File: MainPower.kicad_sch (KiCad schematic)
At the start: 25 parts, among them Q29 MBT2222ADW1T1, Q30 MBT2222ADW1T1, U17 TPS54226PWPR, U18 ADM1176-1ARMZ-R7

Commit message: temp
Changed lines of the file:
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@@
 		)
 	)
-	(hierarchical_label "SDA_BUS"
+	(hierarchical_label "SCL"
 		(shape bidirectional)
-		(at 256.54 130.81 0)
+		(at 256.54 128.27 0)
 		(fields_autoplaced yes)
 		(effects
@@
 		)
 	)
-	(hierarchical_label "SCL_BUS"
+	(hierarchical_label "SDA"
 		(shape bidirectional)
-		(at 256.54 128.27 0)
+		(at 256.54 130.81 0)
 		(fields_autoplaced yes)
 		(effects

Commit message: v1 done
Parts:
- C58, C59: value 100u -> 10u
- U17: symbol Mainboard:TPS54226PWPR -> Argus-IC:TPS54226PWPR
- U18: symbol Mainboard:ADM1176-1ARMZ-R7 -> Argus-IC:ADM1176-1ARMZ-R7
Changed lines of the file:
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@@
 	)
 	(symbol
-		(lib_id "Mainboard:ADM1176-1ARMZ-R7")
+		(lib_id "Argus-IC:ADM1176-1ARMZ-R7")
 		(at 189.23 128.27 0)
 		(unit 1)
@@
 			)
 		)
-		(property "Value" "100u"
+		(property "Value" "10u"
 			(at 37.592 114.808 0)
 			(effects
@@
 			)
 		)
-		(property "Value" "100u"
+		(property "Value" "10u"
 			(at 47.752 114.808 0)
 			(effects
@@
 	)
 	(symbol
-		(lib_id "Mainboard:TPS54226PWPR")
+		(lib_id "Argus-IC:TPS54226PWPR")
 		(at 87.63 127 0)
 		(unit 1)

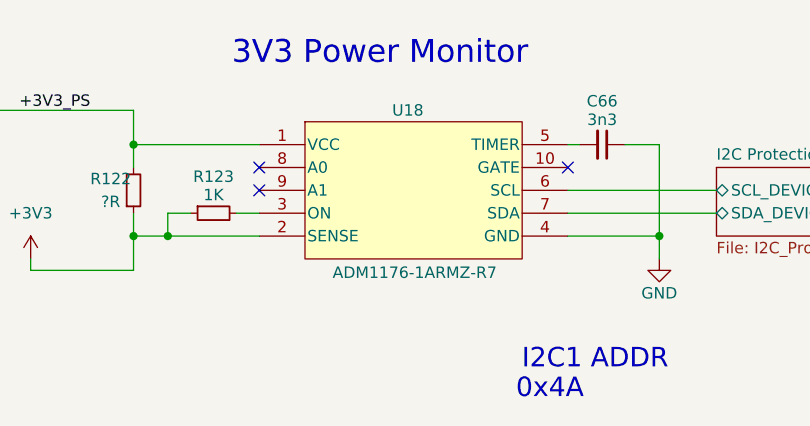
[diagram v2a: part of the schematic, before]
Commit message: Updated i2c device addresses and mcu caps
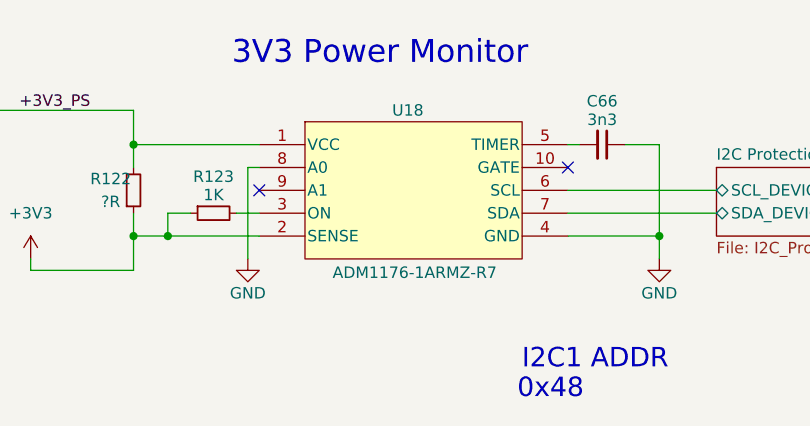
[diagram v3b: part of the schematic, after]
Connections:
- net GND: now also U18.8 (A0)
- no-connect marks 3 -> 2
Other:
- note added: "0x48"
- note removed: "0x4A"
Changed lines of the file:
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@@
 		(at 207.01 125.73)
 	)
-	(no_connect
-		(at 172.72 125.73)
-	)
 	(wire
 		(pts
@@
 	(wire
 		(pts
+			(xy 171.45 125.73) (xy 171.45 135.89)
+		)
+		(stroke
+			(width 0)
+			(type default)
+		)
+	)
+	(wire
+		(pts
 			(xy 142.24 45.72) (xy 142.24 46.99)
 		)
@@
 		(pts
 			(xy 217.17 123.19) (xy 217.17 133.35)
+		)
+		(stroke
+			(width 0)
+			(type default)
+		)
+	)
+	(wire
+		(pts
+			(xy 172.72 125.73) (xy 171.45 125.73)
 		)
 		(stroke
@@
 		)
 	)
-	(text "0x4A"
+	(text "0x48"
 		(exclude_from_sim no)
 		(at 208.788 151.638 0)
@@
 					(unit 1)
 				)
+			)
+		)
+	)
+	(symbol
+		(lib_id "power:GND")
+		(at 171.45 135.89 0)
+		(unit 1)
+		(exclude_from_sim no)
+		(in_bom yes)
+		(on_board yes)
+		(dnp no)
+		(property "Reference" "#PWR0155"
+			(at 171.45 142.24 0)
+			(effects
+				(font
+					(size 1.27 1.27)
+				)
+				(hide yes)
+			)
+		)
+		(property "Value" "GND"
+			(at 171.45 139.7 0)
+			(effects
+				(font
+					(size 1.27 1.27)
+				)
+			)
+		)
+		(property "Footprint" ""
+			(at 171.45 135.89 0)
+			(effects
+				(font
+					(size 1.27 1.27)
+				)
+				(hide yes)
+			)
+		)
+		(property "Datasheet" ""
+			(at 171.45 135.89 0)
+			(effects
+				(font
+					(size 1.27 1.27)
+				)
+				(hide yes)
+			)
+		)
+		(property "Description" "Power symbol creates a global label with name \"GND\" , ground"
+			(at 171.45 135.89 0)
+			(effects
+				(font
+					(size 1.27 1.27)
+				)
+				(hide yes)
+			)
+		)
+		(pin "1"
+		)
+		(instances
+			(project "Avionics-MainBoard"
+				(path "/4c932743-8c6f-426e-9c1f-5a3f2b32c70d/60aa2943-2df4-4541-853f-c25e8e58a8ce"
+					(reference "#PWR0155")
+					(unit 1)
+				)

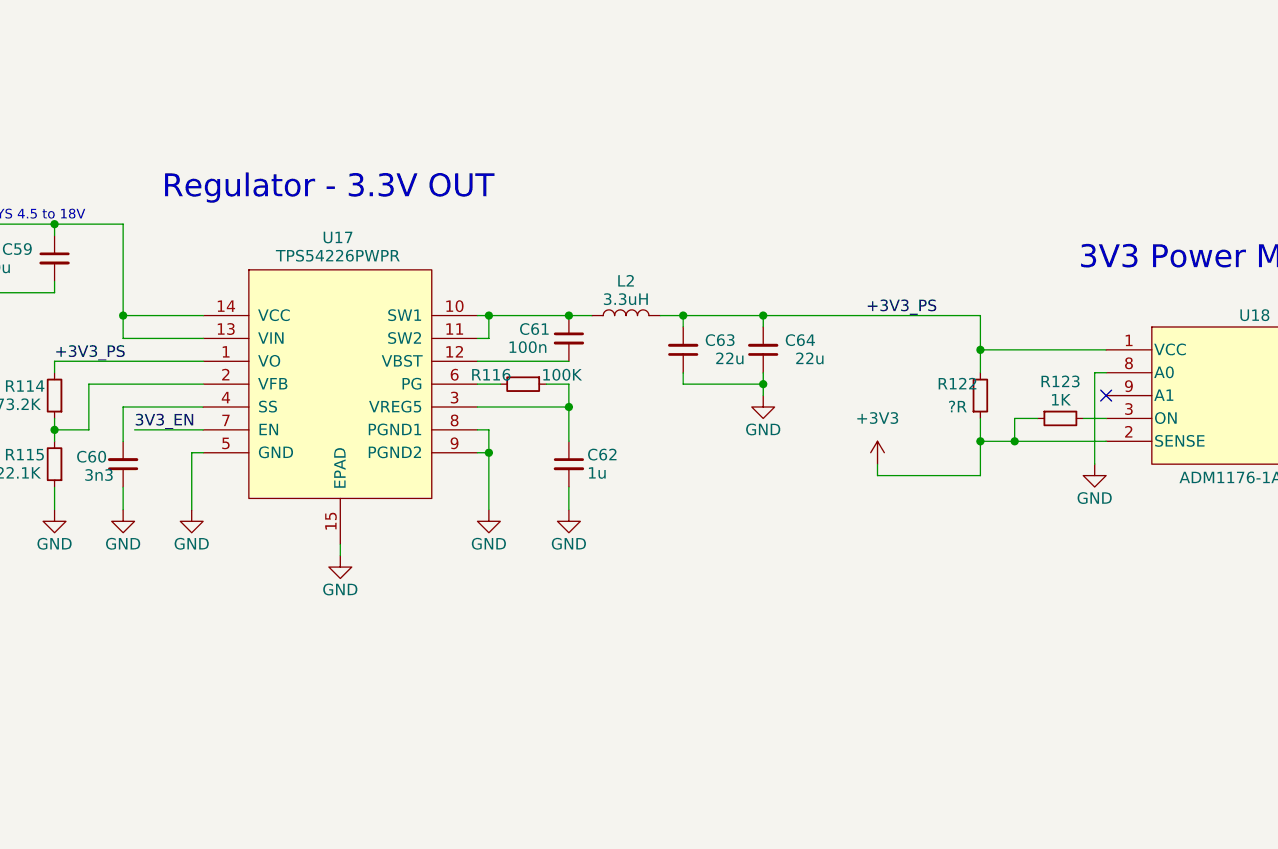
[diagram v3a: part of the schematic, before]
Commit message: Added better protection to SD card, Jetson IO, and added address breakouts to power monitors
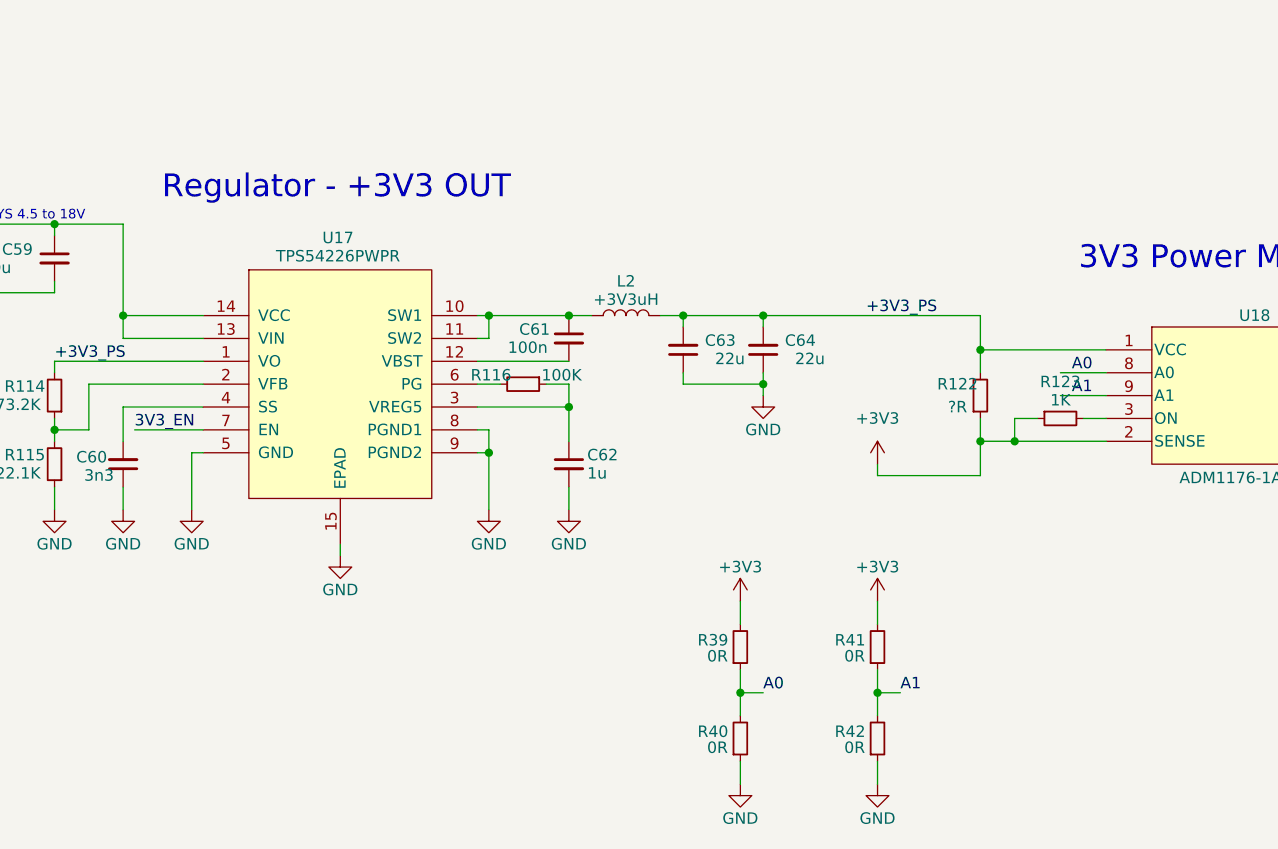
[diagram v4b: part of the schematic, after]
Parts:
- added R39, R40, R41, R42: 0R, Resistor_SMD:R_0603_1608Metric, symbol Device:R_Small
- L2: value 3.3uH -> +3V3uH
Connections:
- net +3V3: now also R39.2, R41.2
- net GND: now also R40.1, R42.1; no longer U18.8 (A0)
- net A1: now reaches U18.9 (A1)
- net A1: now also R41.1, R42.2
- new net A0: R39.1, R40.2, U18.8 (A0)
- no-connect marks 2 -> 1
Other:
- note added: "Regulator - +3V3 OUT"
- note removed: "Regulator - 3.3V OUT"

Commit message: Updated version to v2.1
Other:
- company: (none) -> Carnegie Mellon University
- title: (none) -> Argus Mainboard
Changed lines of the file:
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@@
 	(generator_version "8.0")
 	(paper "A4")
+	(title_block
+		(title "Argus Mainboard")
+		(date "2024-11-19")
+		(rev "v2.1")
+		(company "Carnegie Mellon University")
+		(comment 1 "M. Holliday")
+		(comment 2 "N. Khera")
+		(comment 3 "V. Rajesh")
+	)
 	(junction
 		(at 104.14 134.62)

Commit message: v3 partial schematic updates
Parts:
- added C71, C74, C81: 1u, Capacitor_SMD:C_0603_1608Metric, symbol Device:C_Small
- added C72, C75: 22u, Capacitor_SMD:C_1210_3225Metric, symbol Device:C_Small
- added C73, C76: 10n, Capacitor_SMD:C_0603_1608Metric, symbol Device:C_Small
- added C77, C78: 10u, Capacitor_SMD:C_0805_2012Metric, symbol Device:C_Small
- added C79, C84: 3n3, Capacitor_SMD:C_0603_1608Metric, symbol Device:C_Small
- added C80: 100n, Capacitor_SMD:C_0603_1608Metric, symbol Device:C_Small
- added C82, C83: 22u, Capacitor_SMD:C_0603_1608Metric, symbol Device:C_Small
- added D10, D11: SZMMSZ4685T1G, symbol Device:D_Zener_Small
- added D6, D7, D8, D9: LED_G_0603_LTST-C190GKT, LED_SMD:LED_0603_1608Metric, symbol Device:LED_Small_Filled
- added L3: 3.3uH, Inductor_SMD:L_1812_4532Metric, symbol Device:L
- added R125: 22.1k, Resistor_SMD:R_0603_1608Metric, symbol Device:R_Small
- added R126: 100k, Resistor_SMD:R_0603_1608Metric, symbol Device:R_Small
- added R127: 0.1R, Resistor_SMD:R_2512_6332Metric, symbol Device:R_Small
- added R128: 1k, Resistor_SMD:R_0603_1608Metric, symbol Device:R_Small
- added R129, R130, R131, R132: 0R, Resistor_SMD:R_0603_1608Metric, symbol Device:R_Small
- added R145, R146: 10k, Resistor_SMD:R_0603_1608Metric, symbol Device:R_Small
- added R147, R148: 4.7k, Resistor_SMD:R_0603_1608Metric, symbol Device:R_Small
- added R77: 16k, Resistor_SMD:R_0603_1608Metric, symbol Device:R_Small
- added R78: 3.6k, Resistor_SMD:R_0603_1608Metric, symbol Device:R_Small
- added R79: 51k, Resistor_SMD:R_0603_1608Metric, symbol Device:R_Small
- added R80, R82: 1.54k, Resistor_SMD:R_0603_1608Metric, symbol Device:R_Small
- added R81: 11k, Resistor_SMD:R_0603_1608Metric, symbol Device:R_Small
- added R99: 73.2k, Resistor_SMD:R_0603_1608Metric, symbol Device:R_Small
- added U12, U13: TPS259621DDA, Package_SO:Texas_R-PDSO-G8_EP2.95x4.9mm_Mask2.4x3.1mm_ThermalVias, symbol oresat-ics:TPS259621DDA
- added U19: TPS54226PWPR, Package_SO:HTSSOP-14-1EP_4.4x5mm_P0.65mm_EP3.4x5mm_Mask3x3.1mm, symbol Argus-IC:TPS54226PWPR
- added U21: ADM1176-1ARMZ-R7, Package_SO:MSOP-10_3x3mm_P0.5mm, symbol Argus-IC:ADM1176-1ARMZ-R7
- L2: value +3V3uH -> 3.3uH
- R114, R117: value 73.2K -> 73.2k
- R115: value 22.1K -> 22.1k
- R116, R118, R121: value 100K -> 100k
- R119: value 20K -> 20k
- R120: value 200K -> 200k
- R122: value ?R -> 0.1R
- R123: value 1K -> 1k
- R124: value 10K -> 10k
- R39, R41, R42: now not fitted
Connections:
- net +3V3_PS: now also C82.2, C83.2, D11.1 (K), L3.2, R127.2, R148.2, R99.2, U19.1 (VO), U21.1 (VCC); no longer C63.2, C64.2, L2.2, R114.2, R122.2, U17.1 (VO), U18.1 (VCC)
- net A0: now also R129.1, R130.2, U21.8 (A0)
- net A1: now also R131.1, R132.2, U21.9 (A1)
- net GND: now also C71.2, C72.2, C73.2, C74.2, C75.2, C76.2, C77.2, C78.2, C79.1, C81.2, C82.1, C83.1, C84.1, D10.2 (A), D11.2 (A), D6.1 (K), D7.1 (K), D8.1 (K), D9.1 (K), R125.1, R130.1, R132.1, R78.2, R80.2, R81.2, R82.2, U12.1 (GND), U12.9 (GND), U13.1 (GND), U13.9 (GND), U19.15 (EPAD), U19.5 (GND), U19.8 (PGND1), U19.9 (PGND2), U21.4 (GND)
- net VSYS: now also C71.1, C72.1, C74.1, C75.1, R77.1, R79.1, U12.4 (IN), U13.4 (IN); no longer C58.1, C59.1, U17.13 (VIN), U17.14 (VCC)
- net +3V3 renamed +3V3_M
- net 3V3_EN renamed 3V3_M_EN
- net 3V3_RST renamed 3V3_M_RST
- new net: C79.2, U19.4 (SS)
- new net: R79.2, R81.1, U13.3 (EN/UVLO)
- new net: R77.2, R78.1, U12.3 (EN/UVLO)
- new net: D9.2 (A), R148.1
- new net: C76.1, U13.2 (dVdt)
- new net: C73.1, U12.2 (dVdt)
- new net: D6.2 (A), R145.1
- new net: C81.1, R126.1, U19.3 (VREG5)
- new net: R126.2, U19.6 (PG)
- new net: R125.2, R99.1, U19.2 (VFB)
- new net: D8.2 (A), R147.1
- new net: R80.1, U12.7 (ILM)
- new net: C84.2, U21.5 (TIMER)
- new net: R128.2, U21.3 (ON)
- new net: C80.1, L3.1, U19.10 (SW1), U19.11 (SW2)
- new net: C80.2, U19.12 (VBST)
- new net: R82.1, U13.7 (ILM)
- new net: D7.2 (A), R146.1
- new net +3V3_MS: C63.2, C64.2, D10.1 (K), L2.2, R114.2, R122.2, R147.2, U17.1 (VO), U18.1 (VCC)
- new net +3V3_P: R127.1, R128.1, R129.2, R131.2, U21.2 (SENSE)
- new net 3V3_P_EN: U19.7 (EN)
- new net I2C Protection7/SCL_DEVICE: U21.6 (SCL)
- new net I2C Protection7/SDA_DEVICE: U21.7 (SDA)
- new net VSYS_M: C58.1, C59.1, R145.2, U12.5 (OUT), U17.13 (VIN), U17.14 (VCC)
- new net VSYS_P: C77.1, C78.1, R146.2, U13.5 (OUT), U19.13 (VIN), U19.14 (VCC)
- no-connect marks 1 -> 6
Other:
- added sheet I2C Protection7 (I2C_Protection.kicad_sch)
- note added: "+3V3 Main Power Monitor"
- note added: "+3V3 Main Regulator"
- note added: "+3V3 Main eFuse"
- note added: "+3V3 Peripheral Power Monitor"
- note added: "+3V3 Peripheral Regulator"
- note added: "+3V3 Peripheral eFuse"
- note added: "0x4A"
- note added: "POWER ON"
- note added: "POWER SAFETY"
- note added: "Rsense"
- note added: "TODO: ILIM should be lower"
- note added: "TODO: ILIM should maybe be higher TODO: USE FLT"
- note added: "TODO: Maybe use ADM1176 GATE + NMOS for OC protection"
- note added: "TPS259621 = Autoretry after thermal shutdown Card current limited to 0.6 A by R_ILM = 1.54k ohm dv/dt = 10nF sets it to 4.2 V/ms instead of the default 70 V/ms OVLO = 13.7 V (open) UVLO = 6.0 V"
- note added: "TPS259621 = Autoretry after thermal shutdown Card current limited to 0.6 A by R_ILM = 1.54k ohm dv/dt = 10nF sets it to 4.2 V/ms instead of the default 70 V/ms OVLO = 13.7 V (open) UVLO = 6.2 V"
- note added: "VGOOD"
- note added: "V_z = 3.6V"
- note added: "Vout = 0.765 * (1 + R114 / R115) Vout = 0.765 * (1 + 73.2k / 22.1k) Vout - 3.298V"
- note removed: "3V3 Power Monitor"
- note removed: "Regulator - +3V3 OUT"
- moved on the sheet: C58, C59, C60, C61, C62, C63, C64, C65, C66, L2, Q29A, Q29B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

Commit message: v3 Layout complete
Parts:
- removed R129, R131, R39, R41: 0R, Resistor_SMD:R_0603_1608Metric, symbol Device:R_Small
- added R160: 10k, Resistor_SMD:R_0603_1608Metric, symbol Device:R_Small
- C31: renamed from C71; value 1u -> 22u; footprint Capacitor_SMD:C_0603_1608Metric -> Capacitor_SMD:C_1210_3225Metric
- C32: renamed from C72; value 22u -> 1u; footprint Capacitor_SMD:C_1210_3225Metric -> Capacitor_SMD:C_0603_1608Metric
- C39: renamed from C63; footprint Capacitor_SMD:C_0603_1608Metric -> Capacitor_SMD:C_1210_3225Metric
- C40: renamed from C64; footprint Capacitor_SMD:C_0603_1608Metric -> Capacitor_SMD:C_1210_3225Metric
- C42: renamed from C74; value 1u -> 22u; footprint Capacitor_SMD:C_0603_1608Metric -> Capacitor_SMD:C_1210_3225Metric
- C43: renamed from C75; value 22u -> 1u; footprint Capacitor_SMD:C_1210_3225Metric -> Capacitor_SMD:C_0603_1608Metric
- C50: renamed from C82; footprint Capacitor_SMD:C_0603_1608Metric -> Capacitor_SMD:C_1210_3225Metric
- C51: renamed from C83; footprint Capacitor_SMD:C_0603_1608Metric -> Capacitor_SMD:C_1210_3225Metric
- C53: renamed from C65; footprint Capacitor_SMD:C_0603_1608Metric -> Capacitor_SMD:C_0805_2012Metric
- D7: renamed from D10; footprint (none) -> Diode_SMD:D_SOD-123
- D8: renamed from D11; footprint (none) -> Diode_SMD:D_SOD-123
- L2, L3: footprint Inductor_SMD:L_1812_4532Metric -> Argus-Passives:IND_SPM5030T-3R3M-HZ
- R21: renamed from R78; value 3.6k -> 3k6
- R22: renamed from R80; value 1.54k -> 1k54
- R23: renamed from R114; value 73.2k -> 73k2
- R24: renamed from R115; value 22.1k -> 22k1
- R26: renamed from R122; value 0.1R -> 0.01R
- R31: renamed from R42; now fitted
- R34: renamed from R82; value 1.54k -> 1k54
- R35: renamed from R99; value 73.2k -> 73k2
- R36: renamed from R125; value 22.1k -> 22k1
- R38: renamed from R127; value 0.1R -> 0.01R
- R41: renamed from R130; value 0R -> 150k; now fitted
- R43: renamed from R132; now fitted
- R46: renamed from R147; value 4.7k -> 4k7
- R47: renamed from R148; value 4.7k -> 4k7
- R48: renamed from R117; value 73.2k -> 73k2
- U5: renamed from U12; symbol oresat-ics:TPS259621DDA -> Argus-IC:TPS259621DDA
- U8: renamed from U13; symbol oresat-ics:TPS259621DDA -> Argus-IC:TPS259621DDA
- renumbered C73 to C33, C58 to C34, C59 to C35, C60 to C36, C61 to C37, C62 to C38, C66 to C41, C76 to C44, C77 to C45, C78 to C46, C79 to C47, C80 to C48, C81 to C49, C84 to C52, D6 to D3, D7 to D4, D8 to D5, D9 to D6, Q29 to Q2, Q30 to Q3, R77 to R20, R116 to R25, R123 to R27, R40 to R29, R79 to R32, R81 to R33, R126 to R37, R128 to R39, R145 to R44, R146 to R45, R118 to R49, R120 to R50, R121 to R51, R119 to R52, R124 to R53, U21 to U10, U17 to U6, U18 to U7, U19 to U9
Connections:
- net +3V3_M: now also R160.1
- net 3V3_P_FLT: now reaches U8.6 (*FLT)
- net 3V3_P_FLT: now also R160.2
- net A0 renamed A0_M
- net A0_M: no longer R41.2, U10.8 (A0)
- net A1 renamed A1_M
- net A1_M: no longer R43.2, U10.9 (A1)
- new net A0_P: R41.2, U10.8 (A0)
- new net A1_P: R43.2, U10.9 (A1)
- no-connect marks 6 -> 5
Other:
- sheet I2C Protection5 ports: added 3V3; removed none
- sheet I2C Protection7 ports: added 3V3; removed none
- note added: "0x40"
- note added: "0x41"
- note added: "TODO: ILIM should maybe be higher"
- note removed: "0x48"
- note removed: "0x4A"
- note removed: "TODO: ILIM should maybe be higher TODO: USE FLT"
- note removed: "TODO: Maybe use ADM1176 GATE + NMOS for OC protection"

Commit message: Addressed design issues
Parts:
- R34: value 1k54 -> 909R
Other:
- note added: "TPS259621 = Autoretry after thermal shutdown Card current limited to 1.0 A by R_ILM = 909 ohm dv/dt = 10nF sets it to 4.2 V/ms instead of the default 70 V/ms OVLO = 13.7 V (open) UVLO = 6.2 V"
- note removed: "TODO: ILIM should be lower"
- note removed: "TODO: ILIM should maybe be higher"
- note removed: "TPS259621 = Autoretry after thermal shutdown Card current limited to 0.6 A by R_ILM = 1.54k ohm dv/dt = 10nF sets it to 4.2 V/ms instead of the default 70 V/ms OVLO = 13.7 V (open) UVLO = 6.2 V"
- moved on the sheet: R29, R31, R41, R43
